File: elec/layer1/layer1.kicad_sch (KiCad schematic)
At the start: 97 parts

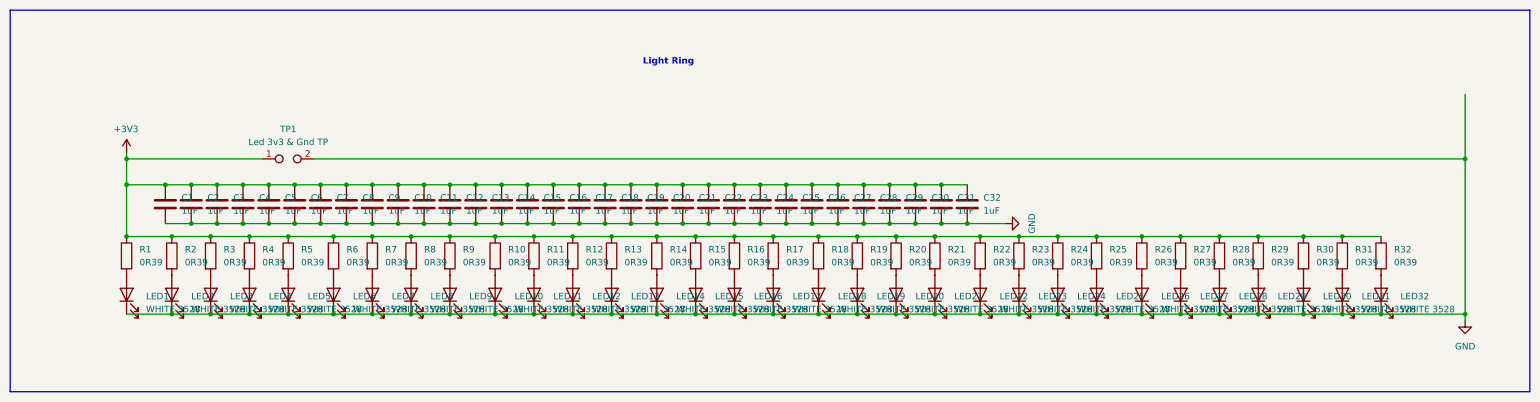
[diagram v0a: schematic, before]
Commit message: feat: light ring
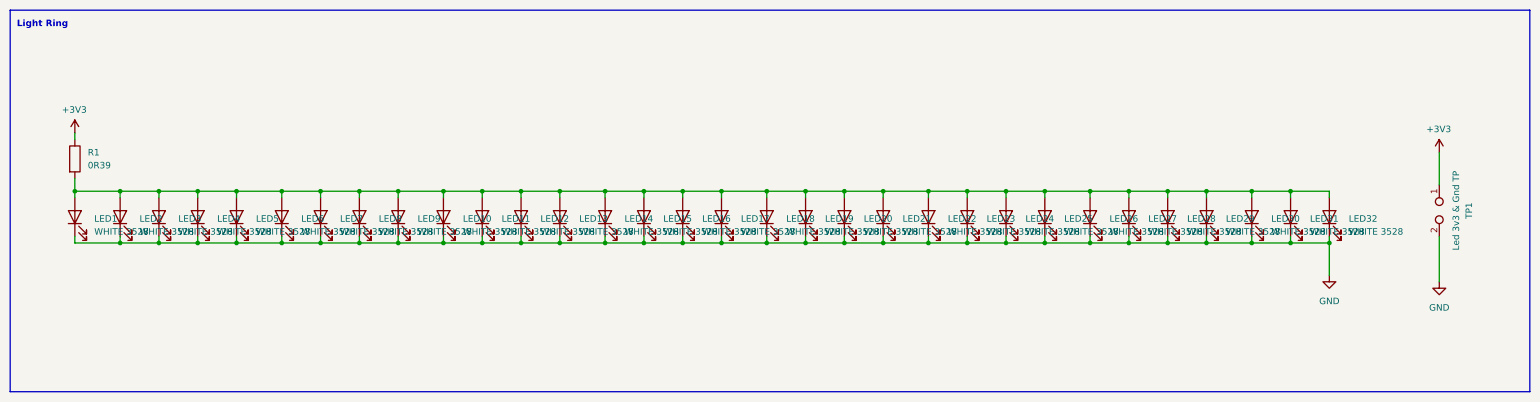
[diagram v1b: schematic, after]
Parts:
- removed C1, C10, C11, C12, C13, C14, C15, C16, C17, C18, C19, C2, C20, C21, C22, C23, C24, C25, C26, C27, C28, C29, C3, C30, C31, C32, C4, C5, C6, C7, C8, C9: 1uF, Capacitor_SMD:C_0603_1608Metric, symbol Device:C
- removed R10, R11, R12, R13, R14, R15, R16, R17, R18, R19, R2, R20, R21, R22, R23, R24, R25, R26, R27, R28, R29, R3, R30, R31, R32, R4, R5, R6, R7, R8, R9: 0R39, Resistor_SMD:R_0603_1608Metric, symbol Device:R
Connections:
- net at LED6.2 (A): now also LED1.2 (A), LED10.2 (A), LED11.2 (A), LED12.2 (A), LED13.2 (A), LED14.2 (A), LED15.2 (A), LED16.2 (A), LED17.2 (A), LED18.2 (A), LED19.2 (A), LED2.2 (A), LED20.2 (A), LED21.2 (A), LED22.2 (A), LED23.2 (A), LED24.2 (A), LED25.2 (A), LED26.2 (A), LED27.2 (A), LED28.2 (A), LED29.2 (A), LED3.2 (A), LED30.2 (A), LED31.2 (A), LED32.2 (A), LED4.2 (A), LED5.2 (A), LED7.2 (A), LED8.2 (A), LED9.2 (A), R1.2
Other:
- moved on the sheet: LED1, LED10, LED11, LED12, LED13, LED14, LED15, LED16, LED17, LED18, LED19, LED2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

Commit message: chore: stupid light ring more
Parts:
- removed R1: 0R39, Resistor_SMD:R_0603_1608Metric, symbol Device:R
- added C33, C34: .1uF, Capacitor_SMD:C_0603_1608Metric, symbol Device:C
- added LED_1, LED_10, LED_11, LED_12, LED_13, LED_14, LED_15, LED_16, LED_17, LED_18, LED_19, LED_2, LED_20, LED_21, LED_22, LED_23, LED_24, LED_25, LED_26, LED_27, LED_28, LED_29, LED_3, LED_30, LED_31, LED_32, LED_4, LED_5, LED_6, LED_7, LED_8, LED_9: R_Photo, Resistor_SMD:R_0603_1608Metric, symbol Device:R_Photo
- added R33, R34: 3k24, Resistor_SMD:R_0603_1608Metric, symbol Device:R
- added R37, R43: 10k, Resistor_SMD:R_0603_1608Metric, symbol Device:R
- added U2, U3: CD74HC4067SM, CD74HC4067SM96G4:SOP65P780X200-24N, symbol 74xx:CD74HC4067SM
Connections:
- net +3V3: now also LED1.2 (A), LED10.2 (A), LED11.2 (A), LED12.2 (A), LED13.2 (A), LED14.2 (A), LED15.2 (A), LED16.2 (A), LED17.2 (A), LED18.2 (A), LED19.2 (A), LED2.2 (A), LED20.2 (A), LED21.2 (A), LED22.2 (A), LED23.2 (A), LED24.2 (A), LED25.2 (A), LED26.2 (A), LED27.2 (A), LED28.2 (A), LED29.2 (A), LED3.2 (A), LED30.2 (A), LED31.2 (A), LED32.2 (A), LED4.2 (A), LED5.2 (A), LED6.2 (A), LED7.2 (A), LED8.2 (A), LED9.2 (A), C33.2, C34.2, LED_1.1, LED_10.1, LED_11.1, LED_12.1, LED_13.1, LED_14.1, LED_15.1, LED_16.1, LED_17.1, LED_18.1, LED_19.1, LED_2.1, LED_20.1, LED_21.1, LED_22.1, LED_23.1, LED_24.1, LED_25.1, LED_26.1, LED_27.1, LED_28.1, LED_29.1, LED_3.1, LED_30.1, LED_31.1, LED_32.1, LED_4.1, LED_5.1, LED_6.1, LED_7.1, LED_8.1, LED_9.1, U2.24 (VCC), U3.24 (VCC)
- net GND: now also C33.1, C34.1, R33.1, R34.1, R37.1, R43.1, U2.12 (GND), U3.12 (GND)
- new net: LED_5.2, U3.5 (I4)
- new net: R37.2, U3.15 (~{E})
- new net: LED_16.2, U3.16 (I15)
- new net: LED_15.2, U3.17 (I14)
- new net: LED_14.2, U3.18 (I13)
- new net: LED_13.2, U3.19 (I12)
- new net: LED_8.2, U3.2 (I7)
- new net: LED_12.2, U3.20 (I11)
- new net: LED_11.2, U3.21 (I10)
- new net: LED_10.2, U3.22 (I9)
- new net: LED_9.2, U3.23 (I8)
- new net: LED_7.2, U3.3 (I6)
- new net: LED_6.2, U3.4 (I5)
- new net: LED_4.2, U3.6 (I3)
- new net: LED_3.2, U3.7 (I2)
- new net: LED_2.2, U3.8 (I1)
- new net: LED_1.2, U3.9 (I0)
- new net: LED_30.2, U2.18 (I13)
- new net: LED_19.2, U2.7 (I2)
- new net: R43.2, U2.15 (~{E})
- new net: LED_24.2, U2.2 (I7)
- new net: LED_20.2, U2.6 (I3)
- new net: LED_23.2, U2.3 (I6)
- new net: LED_31.2, U2.17 (I14)
- new net: LED_22.2, U2.4 (I5)
- new net: LED_17.2, U2.9 (I0)
- new net: LED_21.2, U2.5 (I4)
- new net: LED_18.2, U2.8 (I1)
- new net: LED_26.2, U2.22 (I9)
- new net: LED_32.2, U2.16 (I15)
- new net: LED_29.2, U2.19 (I12)
- new net: LED_28.2, U2.20 (I11)
- new net: LED_27.2, U2.21 (I10)
- new net: LED_25.2, U2.23 (I8)
- new net Mux Com (1-16): R34.2, U3.1 (COM)
- new net Mux Com (17-32): R33.2, U2.1 (COM)
- new net S0: U2.10 (S0), U3.10 (S0)
- new net S1: U2.11 (S1), U3.11 (S1)
- new net S2: U2.14 (S2), U3.14 (S2)
- new net S3: U2.13 (S3), U3.13 (S3)
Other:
- note added: "Ldrs"
- note added: "Mcu"
- moved on the sheet: LED1, LED10, LED11, LED12, LED13, LED14, LED15, LED16, LED17, LED18, LED19, LED2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

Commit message: did l1 light ring partially
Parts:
- U2, U3: footprint CD74HC4067SM96G4:SOP65P780X200-24N -> L1:SOP65P780X200-24N
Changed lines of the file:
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@@
 			)
 		)
-		(property "Footprint" "CD74HC4067SM96G4:SOP65P780X200-24N"
+		(property "Footprint" "L1:SOP65P780X200-24N"
 			(at 148.59 105.41 0)
 			(effects
@@
 			)
 		)
-		(property "Footprint" "CD74HC4067SM96G4:SOP65P780X200-24N"
+		(property "Footprint" "L1:SOP65P780X200-24N"
 			(at 223.52 105.41 0)
 			(effects

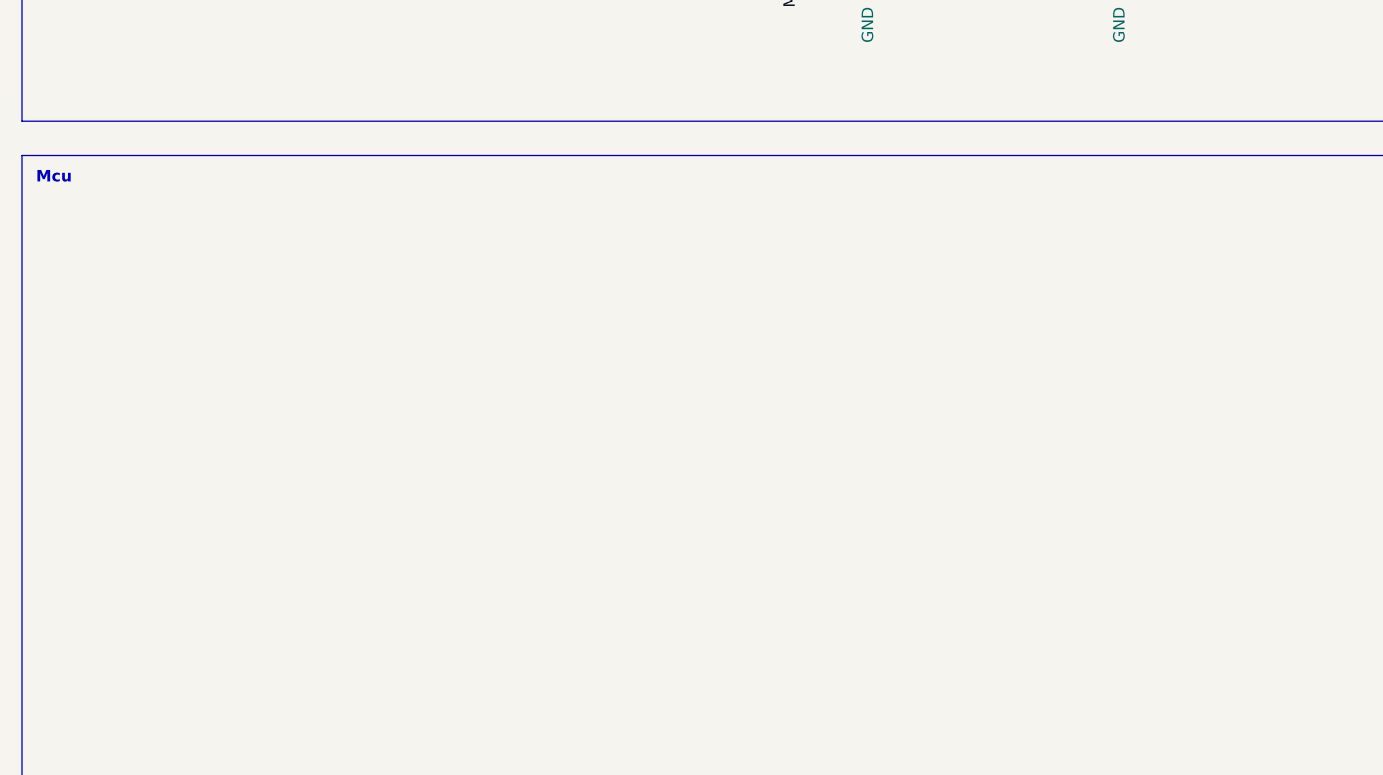
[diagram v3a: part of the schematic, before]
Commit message: added connectors for modules in schmatics
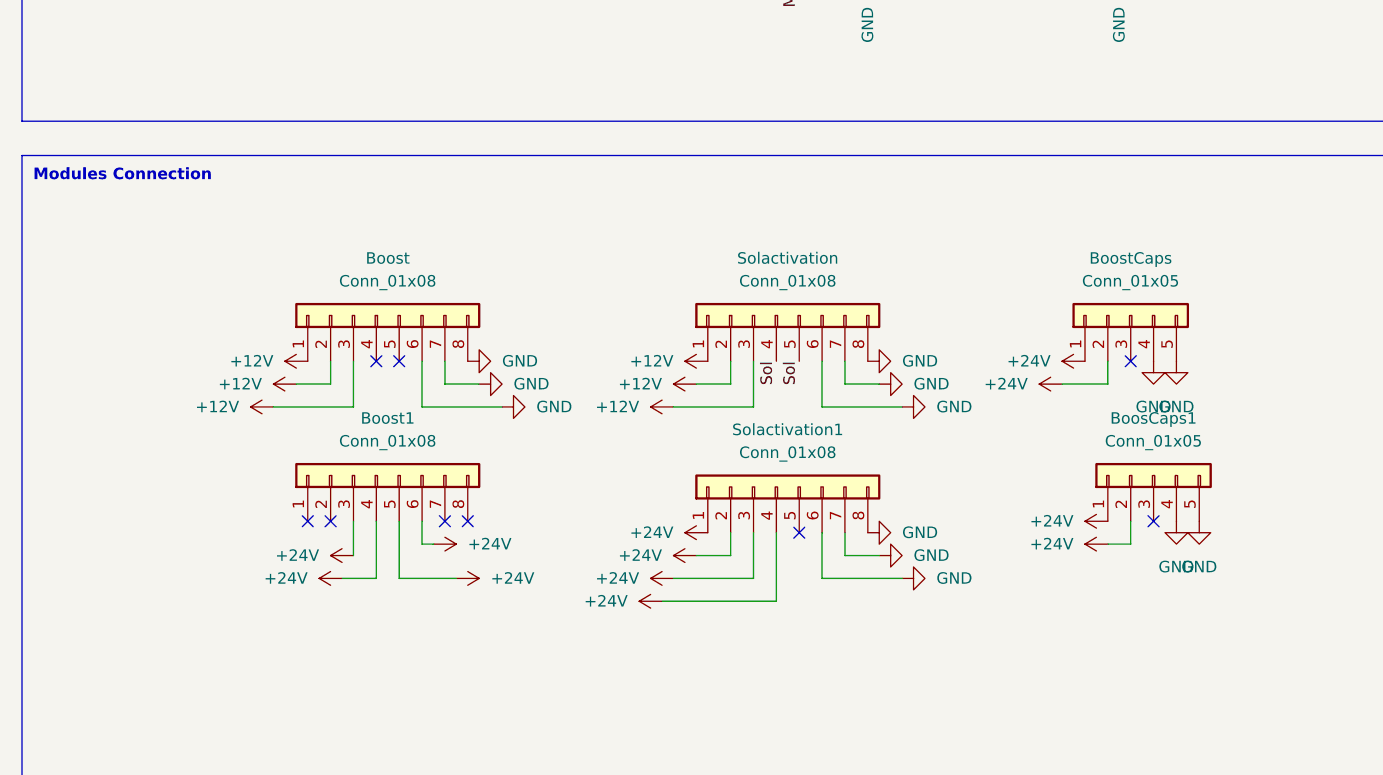
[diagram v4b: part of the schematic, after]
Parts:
- added BoosCaps1, BoostCaps: Conn_01x05, Pinheaders:PinHeader_1x05_P2.54mm_Vertical, symbol Connector_Generic:Conn_01x05
- added Boost, Boost1, Solactivation, Solactivation1: Conn_01x08, symbol Connector_Generic:Conn_01x08
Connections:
- net GND: now also BoosCaps1.4 (Pin_4), BoosCaps1.5 (Pin_5), Boost.6 (Pin_6), Boost.7 (Pin_7), Boost.8 (Pin_8), BoostCaps.4 (Pin_4), BoostCaps.5 (Pin_5), Solactivation.6 (Pin_6), Solactivation.7 (Pin_7), Solactivation.8 (Pin_8), Solactivation1.6 (Pin_6), Solactivation1.7 (Pin_7), Solactivation1.8 (Pin_8)
- new net +12V: Boost.1 (Pin_1), Boost.2 (Pin_2), Boost.3 (Pin_3), Solactivation.1 (Pin_1), Solactivation.2 (Pin_2), Solactivation.3 (Pin_3)
- new net +24V: BoosCaps1.1 (Pin_1), BoosCaps1.2 (Pin_2), Boost1.3 (Pin_3), Boost1.4 (Pin_4), Boost1.5 (Pin_5), Boost1.6 (Pin_6), BoostCaps.1 (Pin_1), BoostCaps.2 (Pin_2), Solactivation1.1 (Pin_1), Solactivation1.2 (Pin_2), Solactivation1.3 (Pin_3), Solactivation1.4 (Pin_4)
- new net Sol: Solactivation.4 (Pin_4), Solactivation.5 (Pin_5)
- no-connect marks 0 -> 9
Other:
- note added: "Modules Connection"
- note removed: "Mcu"

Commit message: mostly done with l1 scchematics
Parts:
- added U1: DEV-15583, DEV-15583:MODULE_DEV-15583, symbol Teensy4.0:DEV-15583
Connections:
- net +3V3: now also U1.3.3V_1, U1.3.3V_2
- net GND: now also U1.G1, U1.G2, U1.G3
- net Mux Com (1-16): now also U1.18
- net Mux Com (17-32): now also U1.19
- net S0: now also U1.14
- net S1: now also U1.15
- net S2: now also U1.16
- net S3: now also U1.17
- net Sol: now also U1.2
- new net +5V: U1.VIN
- no-connect marks 9 -> 28

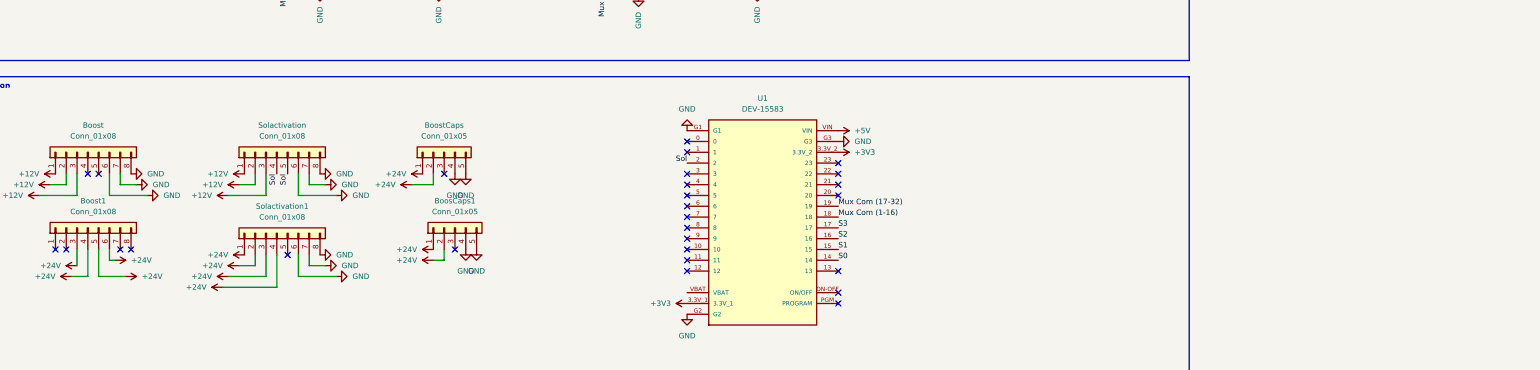
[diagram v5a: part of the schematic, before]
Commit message: l1:added boost measurements
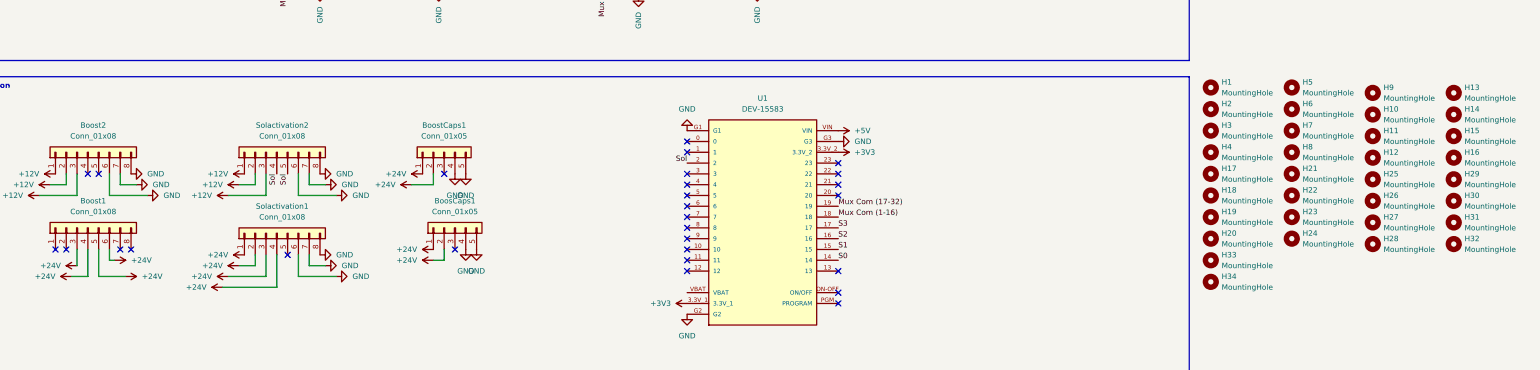
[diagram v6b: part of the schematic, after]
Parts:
- added H1, H2: MountingHole, MountingHole:MountingHole_2.2mm_M2_DIN965_Pad_TopBottom, symbol Mechanical:MountingHole
- added H10, H11, H12, H13, H14, H15, H16, H17, H18, H19, H20, H21, H22, H23, H24, H25, H26, H27, H28, H29, H3, H30, H31, H32, H33, H34, H4, H5, H6, H7, H8, H9: MountingHole, MountingHole:MountingHole_3.2mm_M3_DIN965_Pad_TopBottom, symbol Mechanical:MountingHole
- Boost1, Solactivation1: footprint (none) -> L1:PinHeader_1x08_P2.54mm_Vertical
- Boost2: renamed from Boost; footprint (none) -> L1:PinHeader_1x08_P2.54mm_Vertical
- Solactivation2: renamed from Solactivation; footprint (none) -> L1:PinHeader_1x08_P2.54mm_Vertical
- U1: footprint DEV-15583:MODULE_DEV-15583 -> L1:MODULE_DEV-15583
- renumbered BoostCaps to BoostCaps1

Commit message: almost done maybe
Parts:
- removed BoosCaps1, BoostCaps1: Conn_01x05, Pinheaders:PinHeader_1x05_P2.54mm_Vertical, symbol Connector_Generic:Conn_01x05
- added L1-->L2Connection1, L1-->L2Connection2: Conn_01x08, L1:PinHeader_1x08_P2.54mm_Vertical, symbol Connector_Generic:Conn_01x08
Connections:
- net +12V: now also L1-->L2Connection2.1 (Pin_1), L1-->L2Connection2.2 (Pin_2), L1-->L2Connection2.3 (Pin_3)
- net +3V3: now also L1-->L2Connection1.1 (Pin_1), L1-->L2Connection1.2 (Pin_2), L1-->L2Connection1.3 (Pin_3)
- net GND: now also L1-->L2Connection1.6 (Pin_6), L1-->L2Connection1.7 (Pin_7), L1-->L2Connection1.8 (Pin_8), L1-->L2Connection2.6 (Pin_6), L1-->L2Connection2.7 (Pin_7), L1-->L2Connection2.8 (Pin_8)
- net Mux Com (1-16): now also U1.19; no longer U1.18
- net Mux Com (17-32): now also U1.18; no longer U1.19
- net Sol: now also U1.20; no longer U1.2
- new net RX: L1-->L2Connection2.4 (Pin_4)
- new net TX: L1-->L2Connection2.5 (Pin_5)
- no-connect marks 28 -> 29

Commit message: l1:connected most stuff
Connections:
- net +5V: now also L1-->L2Connection1.4 (Pin_4), L1-->L2Connection1.5 (Pin_5)
- net RX: now also U1.8
- net TX: now also U1.7
- no-connect marks 29 -> 25
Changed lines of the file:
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@@
 	)
 	(no_connect
-		(at 196.85 208.28)
-	)
-	(no_connect
 		(at 196.85 226.06)
 	)
@@
 	)
 	(no_connect
-		(at 147.32 215.9)
-	)
-	(no_connect
 		(at 232.41 200.66)
 	)
@@
 	)
 	(no_connect
-		(at 144.78 215.9)
-	)
-	(no_connect
 		(at 196.85 190.5)
 	)
 	(no_connect
-		(at 196.85 210.82)
-	)
-	(no_connect
 		(at 232.41 198.12)
 	)
@@
 	(wire
 		(pts
+			(xy 147.32 222.25) (xy 147.32 215.9)
+		)
+		(stroke
+			(width 0)
+			(type default)
+		)
+	)
+	(wire
+		(pts
 			(xy 69.85 53.34) (xy 77.47 53.34)
 		)
@@
 	(wire
 		(pts
+			(xy 144.78 222.25) (xy 144.78 215.9)
+		)
+		(stroke
+			(width 0)
+			(type default)
+		)
+	)
+	(wire
+		(pts
 			(xy 111.76 200.66) (xy 107.95 200.66)
 		)
@@
 		)
 	)
+	(label "RX"
+		(at 196.85 210.82 180)
+		(effects
+			(font
+				(size 1.27 1.27)
+			)
+			(justify right bottom)
+		)
+	)
 	(label "S0"
 		(at 120.65 147.32 180)
@@
 	)
 	(label "TX"
+		(at 196.85 208.28 180)
+		(effects
+			(font
+				(size 1.27 1.27)
+			)
+			(justify right bottom)
+		)
+	)
+	(label "TX"
 		(at 148.59 198.12 270)
 		(effects
@@
 	)
 	(symbol
+		(lib_id "power:+5V")
+		(at 147.32 222.25 270)
+		(unit 1)
+		(exclude_from_sim no)
+		(in_bom yes)
+		(on_board yes)
+		(dnp no)
+		(fields_autoplaced yes)
+		(property "Reference" "#PWR058"
+			(at 143.51 222.25 0)
+			(effects
+				(font
+					(size 1.27 1.27)
+				)
+				(hide yes)
+			)
+		)
+		(property "Value" "+5V"
+			(at 151.13 222.2499 90)
+			(effects
+				(font
+					(size 1.27 1.27)
+				)
+				(justify left)
+			)
+		)
+		(property "Footprint" ""
+			(at 147.32 222.25 0)
+			(effects
+				(font
+					(size 1.27 1.27)
+				)
+				(hide yes)
+			)
+		)
+		(property "Datasheet" ""
+			(at 147.32 222.25 0)
+			(effects
+				(font
+					(size 1.27 1.27)
+				)
+				(hide yes)
+			)
+		)
+		(property "Description" "Power symbol creates a global label with name \"+5V\""
+			(at 147.32 222.25 0)
+			(effects
+				(font
+					(size 1.27 1.27)
+				)
+				(hide yes)
+			)
+		)
+		(pin "1"
+		)
+		(instances
+			(project "layer1"
+				(path "/68b2dc84-e8ac-4ad5-a4b5-71d0b0deb0c0"
+					(reference "#PWR058")
+					(unit 1)
+				)
+			)
+		)
+	)
+	(symbol
 		(lib_id "power:+3V3")
 		(at 135.89 218.44 90)
@@
 					(unit 1)
 				)
+			)
+		)
+	)
+	(symbol
+		(lib_id "power:+5V")
+		(at 144.78 222.25 90)
+		(unit 1)
+		(exclude_from_sim no)
+		(in_bom yes)
+		(on_board yes)
+		(dnp no)
+		(fields_autoplaced yes)
+		(property "Reference" "#PWR057"
+			(at 148.59 222.25 0)
+			(effects
+				(font
+					(size 1.27 1.27)
+				)
+				(hide yes)
+			)
+		)
+		(property "Value" "+5V"
+			(at 140.97 222.2499 90)
+			(effects
+				(font
+					(size 1.27 1.27)
+				)
+				(justify left)
+			)
+		)
+		(property "Footprint" ""
+			(at 144.78 222.25 0)
+			(effects
+				(font
+					(size 1.27 1.27)
+				)
+				(hide yes)
+			)
+		)
+		(property "Datasheet" ""
+			(at 144.78 222.25 0)
+			(effects
+				(font
+					(size 1.27 1.27)
+				)
+				(hide yes)
+			)
+		)
+		(property "Description" "Power symbol creates a global label with name \"+5V\""
+			(at 144.78 222.25 0)
+			(effects
+				(font
+					(size 1.27 1.27)
+				)
+				(hide yes)
+			)
+		)
+		(pin "1"
+		)
+		(instances
+			(project ""
+				(path "/68b2dc84-e8ac-4ad5-a4b5-71d0b0deb0c0"
+					(reference "#PWR057")
+					(unit 1)
+				)
